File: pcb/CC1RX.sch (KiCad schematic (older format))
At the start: 108 parts, among them J1 Phones - 3.5mm Stereo, P1 XTAL GND, P2 BFO, Q1 2N7002, Q2 2N7002, Q3 2N7002, Q4 BF998, Q5 MMBFJ310, Q6 MMBFJ310, Q7 BF998, Q8 MMBFJ310, T1 FT37-61 33T:3T, T2 FT37-61 33T:3T, U1 NE5532, X1 6.144 MHz, X2 6.144 MHz, X3 6.144 MHz, X4 6.144 MHz, X5 6.144 MHz

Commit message: Update schematics for beta
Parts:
- C11: value 1u MLCC -> 4.7u MLCC
- C34: value 100n -> 10
- C37: value 100n -> 10n
- Q4, Q7: value BF998 -> BF991
- R15, R24: value 2.7k -> 10k
- R35: value 220 -> 470
- R5, R7: value 33k -> 100k
- R6: value 33k -> 1M
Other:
- note added: "All capacitors in pF unless specified"
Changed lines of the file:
@@
-EESchema Schematic File Version 2  date Wed 09 Jan 2013 07:00:57 PM PST
+EESchema Schematic File Version 2  date Thu 31 Jan 2013 03:10:17 PM PST
 LIBS:NT7S
 LIBS:power
@@
 Sheet 2 3
 Title "CC1 Transceiver"
-Date "10 jan 2013"
+Date "31 jan 2013"
 Rev "A"
 Comp "Etherkit"
@@
 P 3900 3975
 F 0 "Q4" H 4120 4030 50  0000 R CNN
-F 1 "BF998" H 4265 3935 50  0000 R CNN
+F 1 "BF991" H 4265 3935 50  0000 R CNN
 	1    3900 3975
 	1    0    0    -1
@@
 P 8710 2110
 F 0 "Q7" H 8945 2060 50  0000 R CNN
-F 1 "BF998" H 9090 1970 50  0000 R CNN
+F 1 "BF991" H 9090 1970 50  0000 R CNN
 	1    8710 2110
 	1    0    0    -1
@@
 P 8810 2520
 F 0 "R35" H 8665 2530 50  0000 C CNN
-F 1 "220" H 8665 2455 50  0000 C CNN
+F 1 "470" H 8665 2455 50  0000 C CNN
 	1    8810 2520
 	1    0    0    -1
@@
 P 9035 2010
 F 0 "C37" H 9210 1965 50  0000 C CNN
-F 1 "100n" H 9240 1885 50  0000 C CNN
+F 1 "10n" H 9205 1895 50  0000 C CNN
 	1    9035 2010
 	1    0    0    -1
@@
 P 8860 3990
 F 0 "C34" V 8640 3990 50  0000 C CNN
-F 1 "100n" V 8720 4010 50  0000 C CNN
+F 1 "10" V 8720 4010 50  0000 C CNN
 	1    8860 3990
 	0    1    1    0
@@
 P 3060 6315
 F 0 "R5" V 2950 6305 50  0000 C CNN
-F 1 "33k" V 2875 6285 50  0000 C CNN
+F 1 "100k" V 2875 6285 50  0000 C CNN
 	1    3060 6315
 	0    -1   -1   0
@@
 P 3330 6570
 F 0 "R7" H 3455 6580 50  0000 C CNN
-F 1 "33k" H 3475 6505 50  0000 C CNN
+F 1 "100k" H 3495 6510 50  0000 C CNN
 	1    3330 6570
 	1    0    0    -1
@@
 P 3625 6425
 F 0 "C11" H 3805 6455 50  0000 C CNN
-F 1 "1u MLCC" H 3900 6380 50  0000 C CNN
+F 1 "4.7u MLCC" H 3930 6380 50  0000 C CNN
 	1    3625 6425
 	1    0    0    -1
@@
 P 4540 6505
 F 0 "R15" H 4690 6515 50  0000 C CNN
-F 1 "2.7k" H 4700 6440 50  0000 C CNN
+F 1 "10k" H 4680 6440 50  0000 C CNN
 	1    4540 6505
 	1    0    0    -1
@@
 P 6275 6555
 F 0 "R24" H 6415 6565 50  0000 C CNN
-F 1 "2.7k" H 6430 6490 50  0000 C CNN
+F 1 "10k" H 6410 6490 50  0000 C CNN
 	1    6275 6555
 	1    0    0    -1
@@
 P 3330 6060
 F 0 "R6" H 3455 6070 50  0000 C CNN
-F 1 "33k" H 3475 5995 50  0000 C CNN
+F 1 "1M" H 3475 5995 50  0000 C CNN
 	1    3330 6060
 	1    0    0    -1
@@
 Wire Wire Line
 	6360 3650 6360 3600
+Text Notes 8730 6985 0    60   ~ 0
+All capacitors in pF unless specified
 $EndSCHEMATC

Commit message: Beta test 1
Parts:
- removed T2: FT37-61 33T:3T, symbol XMFR-STEPDOWN
- C21, C24, C28: value 180 -> 120
- C22, C27: value 150 -> 100
- C34: value 10 -> 33
- C39, C40: value 100 -> 33
- L6: value 1u -> 22u
- Q4, Q7: value BF991 -> BF998
- R15, R24: value 10k -> 4.7k
- R19, R29: value 22 -> 10
- R20, R30: value 220 -> 1k
- R27: value 2.2k -> 220
- R32: value 100k -> 2.2k
- R34: value 10k -> 2.2k
- T1: value FT37-61 33T:3T -> FT37-43 20T:5T
- X5: value 6.144 MHz -> 4.9152 MHz
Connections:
- net at C28.1: now also Q6.2 (G), R27.1
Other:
- note added: "440 Hz BW\nZ=250 ohms\nAll crystals 4.915 MHz"
- note removed: "440 Hz BW\nZ=200 ohms\nAll crystals 6.144 MHz"
- moved on the sheet: C30, C31, C32, C33, C34, C35, C36, C37, C38, C39, C40, C41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

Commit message: Minor correction for Beta 1
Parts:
- C17, C25: value 1u MLCC -> 100n

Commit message: A few more changes on Beta 1
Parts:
- C11: value 4.7u MLCC -> 1u MLCC
- C17: value 100n -> 10n
- C38, C9: value 100n -> 1u MLCC
- R34: value 2.2k -> 10k
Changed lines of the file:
@@
-EESchema Schematic File Version 2  date Sun 24 Feb 2013 04:48:14 PM PST
+EESchema Schematic File Version 2  date Sun 24 Feb 2013 06:59:34 PM PST
 LIBS:NT7S
 LIBS:power
@@
 P 5240 4080
 F 0 "C19" H 5075 4105 50  0000 C CNN
-F 1 "100n" H 5025 4180 50  0000 C CNN
+F 1 "100n" H 5055 4175 50  0000 C CNN
 F 2 "" H 5240 4080 60  0001 C CNN
 F 3 "" H 5240 4080 60  0001 C CNN
@@
 U 1 1 50DE4BA1
 P 5025 3330
-F 0 "R19" H 4910 3370 50  0000 C CNN
-F 1 "10" H 4890 3300 50  0000 C CNN
+F 0 "R19" H 4880 3380 50  0000 C CNN
+F 1 "10" H 4855 3305 50  0000 C CNN
 F 2 "" H 5025 3330 60  0001 C CNN
 F 3 "" H 5025 3330 60  0001 C CNN
@@
 P 8650 1770
 F 0 "R34" H 8490 1820 50  0000 C CNN
-F 1 "2.2k" H 8490 1745 50  0000 C CNN
+F 1 "10k" H 8490 1745 50  0000 C CNN
 F 2 "" H 8650 1770 60  0001 C CNN
 F 3 "" H 8650 1770 60  0001 C CNN
@@
 P 9065 1955
 F 0 "C38" V 8840 1945 50  0000 C CNN
-F 1 "100n" V 8925 1975 50  0000 C CNN
+F 1 "1u MLCC" V 8920 2035 50  0000 C CNN
 F 2 "" H 9065 1955 60  0001 C CNN
 F 3 "" H 9065 1955 60  0001 C CNN
@@
 P 3110 5815
 F 0 "C9" V 2890 5785 50  0000 C CNN
-F 1 "100n" V 2970 5835 50  0000 C CNN
+F 1 "1u MLCC" V 2965 5900 50  0000 C CNN
 F 2 "" H 3110 5815 60  0001 C CNN
 F 3 "" H 3110 5815 60  0001 C CNN
@@
 P 3625 6425
 F 0 "C11" H 3805 6455 50  0000 C CNN
-F 1 "4.7u MLCC" H 3930 6380 50  0000 C CNN
+F 1 "1u MLCC" H 3895 6385 50  0000 C CNN
 F 2 "" H 3625 6425 60  0001 C CNN
 F 3 "" H 3625 6425 60  0001 C CNN
@@
 P 4540 6790
 F 0 "C17" H 4725 6825 50  0000 C CNN
-F 1 "100n" H 4750 6745 50  0000 C CNN
+F 1 "10n" H 4725 6750 50  0000 C CNN
 F 2 "" H 4540 6790 60  0001 C CNN
 F 3 "" H 4540 6790 60  0001 C CNN

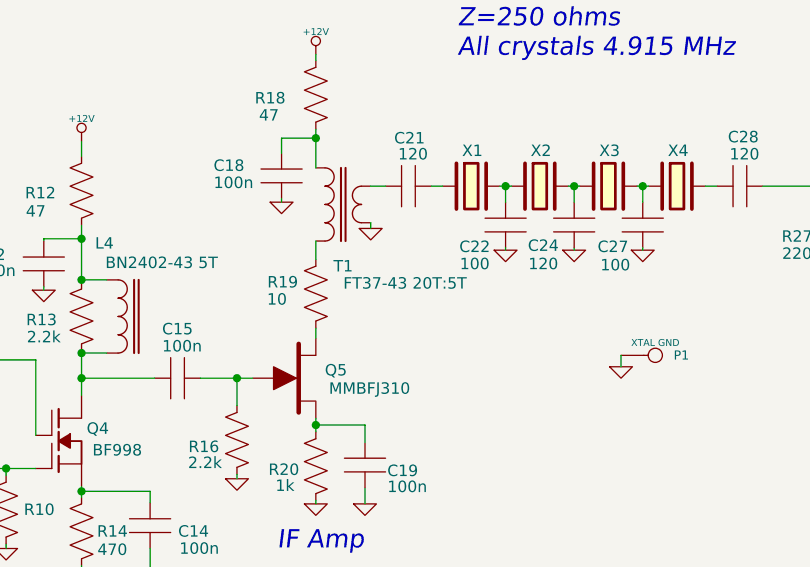
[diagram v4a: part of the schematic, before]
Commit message: Change to T1 and L5 in schematics/BOM
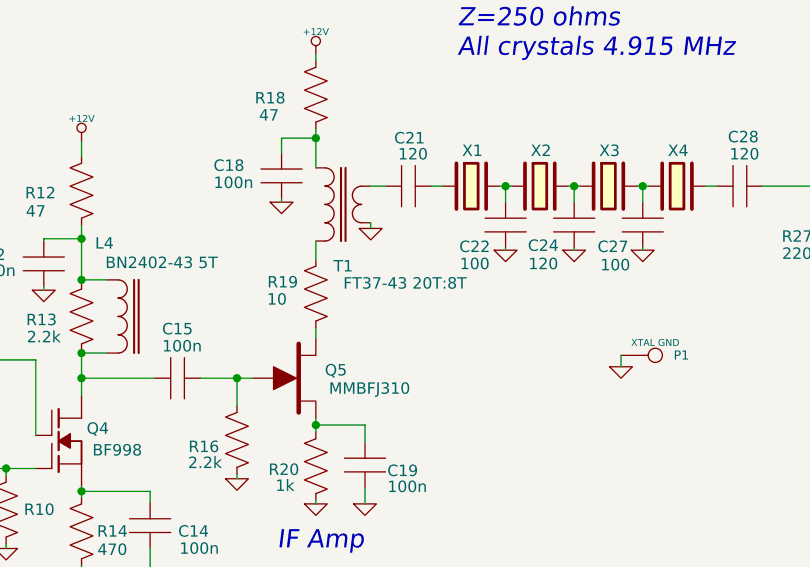
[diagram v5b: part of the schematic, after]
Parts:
- T1: value FT37-43 20T:5T -> FT37-43 20T:8T
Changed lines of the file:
@@
-EESchema Schematic File Version 2  date Sun 24 Feb 2013 06:59:34 PM PST
+EESchema Schematic File Version 2  date Sun 14 Apr 2013 09:43:51 AM PDT
 LIBS:NT7S
 LIBS:power
@@
 Sheet 2 3
 Title "CC1 Transceiver"
-Date "25 feb 2013"
+Date "14 apr 2013"
 Rev "A"
 Comp "Etherkit"
@@
 P 5065 2940
 F 0 "T1" H 5145 2670 50  0000 C CNN
-F 1 "FT37-43 20T:5T" H 5415 2595 50  0000 C CNN
+F 1 "FT37-43 20T:8T" H 5415 2595 50  0000 C CNN
 F 2 "" H 5065 2940 60  0001 C CNN
 F 3 "" H 5065 2940 60  0001 C CNN
